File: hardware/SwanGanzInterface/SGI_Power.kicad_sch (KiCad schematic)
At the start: 21 parts, among them IC1 LM2937ET-3.3_NOPB, IC2 LM2937ET-3.3_NOPB, IC3 LM4041CILPR, U3 OPA2350

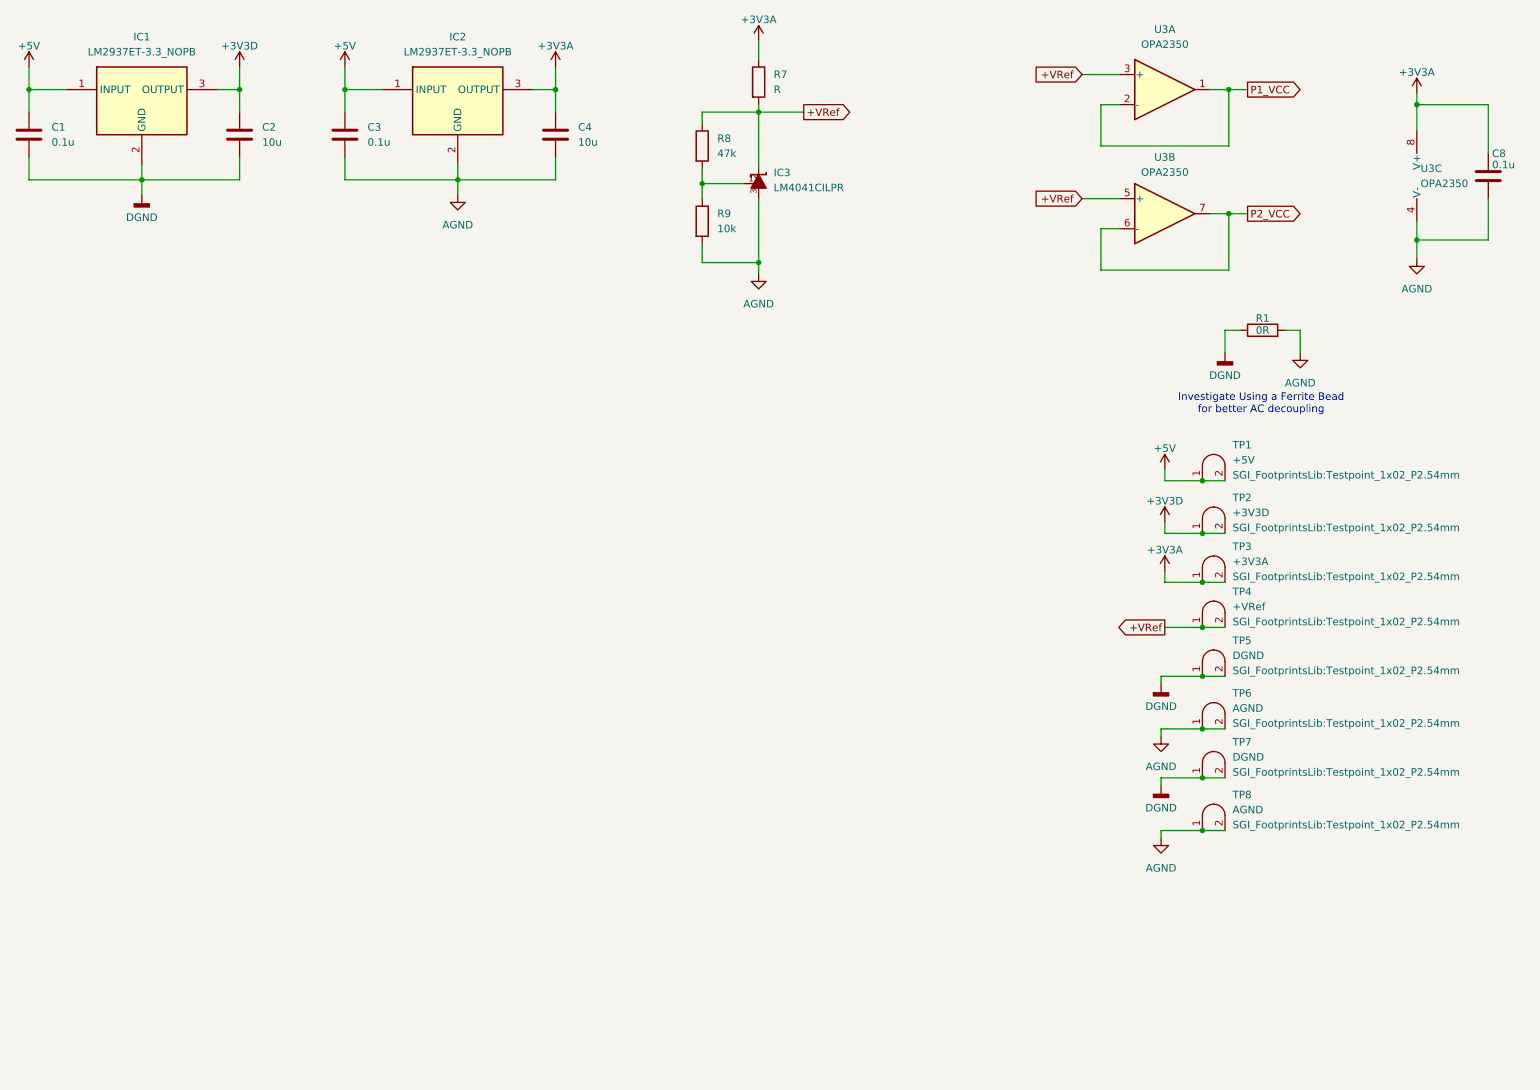
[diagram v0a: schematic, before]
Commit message: Finished MSP-LP Symbol, Started Pressure_Connector Symbol
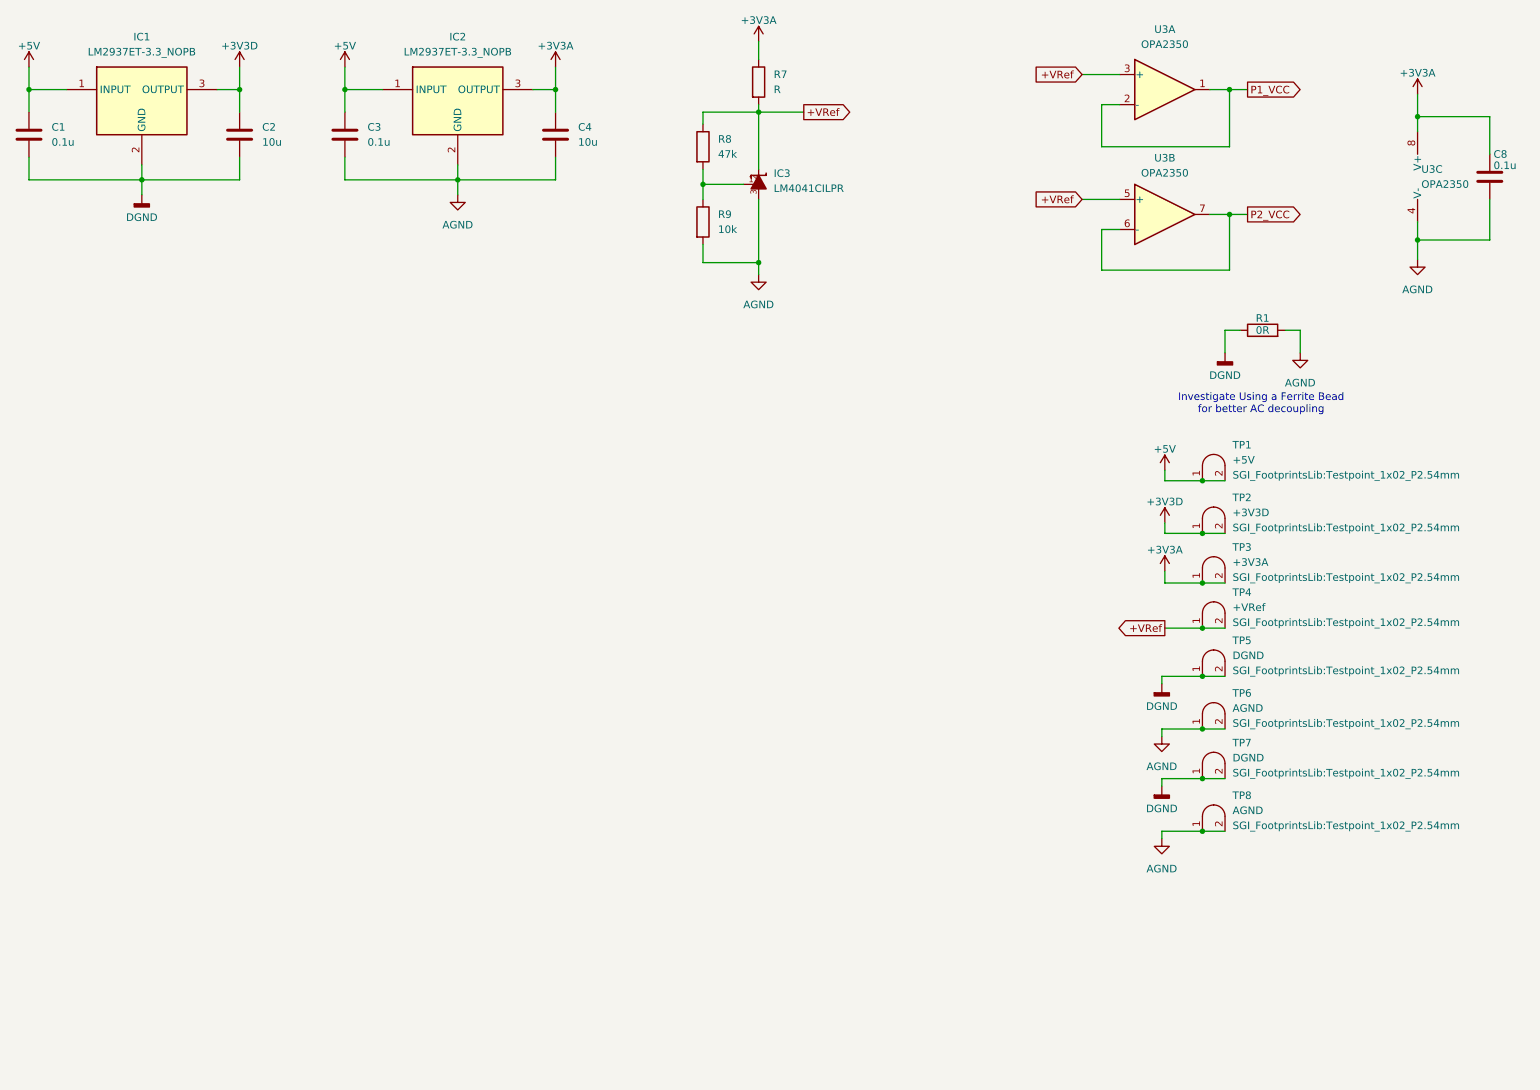
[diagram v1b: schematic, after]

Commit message: Updated gain and added power connector
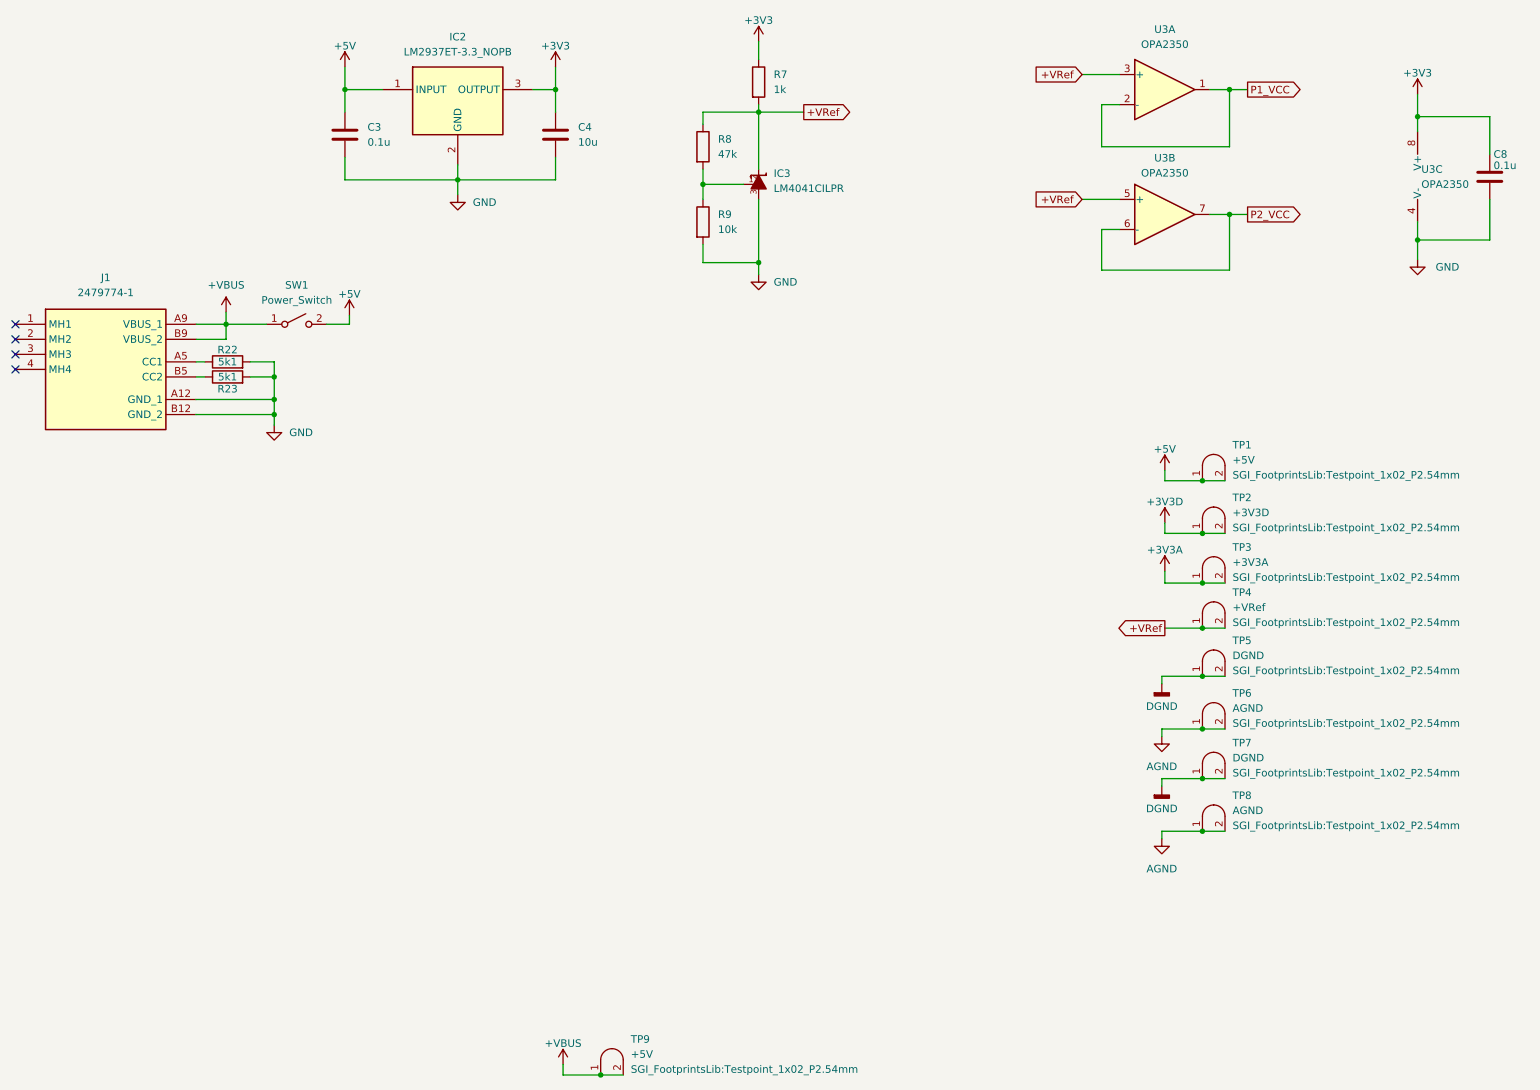
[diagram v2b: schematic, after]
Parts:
- removed C1: 0.1u, symbol Device:C
- removed C2: 10u, symbol Device:C
- removed IC1: LM2937ET-3.3_NOPB, SGI_FootprintsLib:TO254P470X1028X1955-3P, symbol SGI_SymbolLib:LM2937ET-3.3_NOPB
- removed R1: 0R, symbol Device:R
- added J1: 2479774-1, SGI_FootprintsLib:24797741, symbol SGI_SymbolLib:2479774-1
- added R22, R23: 5k1, symbol Device:R
- added SW1: Power_Switch, SGI_FootprintsLib:SW-T3-1A-A-A3-S1, symbol SGI_SymbolLib:Power_Switch
- added TP9: +5V, SGI_FootprintsLib:Testpoint_1x02_P2.54mm, symbol SGI_SymbolLib:Testpoint
- R7: value R -> 1k
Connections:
- net +3V3A: no longer C4.1, C8.1, IC2.3 (OUTPUT), R7.1, U3.8 (V+)
- net +5V: now also SW1.2 (B)
- net AGND: no longer C3.2, C4.2, C8.2, IC2.2 (GND), IC3.3, R9.2, U3.4 (V-)
- new net: J1.A5 (CC1), R22.1
- new net: J1.B5 (CC2), R23.1
- new net +3V3: C4.1, C8.1, IC2.3 (OUTPUT), R7.1, U3.8 (V+)
- new net +VBUS: J1.A9 (VBUS_1), J1.B9 (VBUS_2), SW1.1 (A), TP9.1 (A), TP9.2 (B)
- new net GND: C3.2, C4.2, C8.2, IC2.2 (GND), IC3.3, J1.A12 (GND_1), J1.B12 (GND_2), R22.2, R23.2, R9.2, U3.4 (V-)
- no-connect marks 0 -> 4
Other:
- note removed: "Investigate Using a Ferrite Bead for better AC decoupling"

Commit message: Reverse Polarity Fet, Updated Notes, Added second gain stage for pressure, General Updates
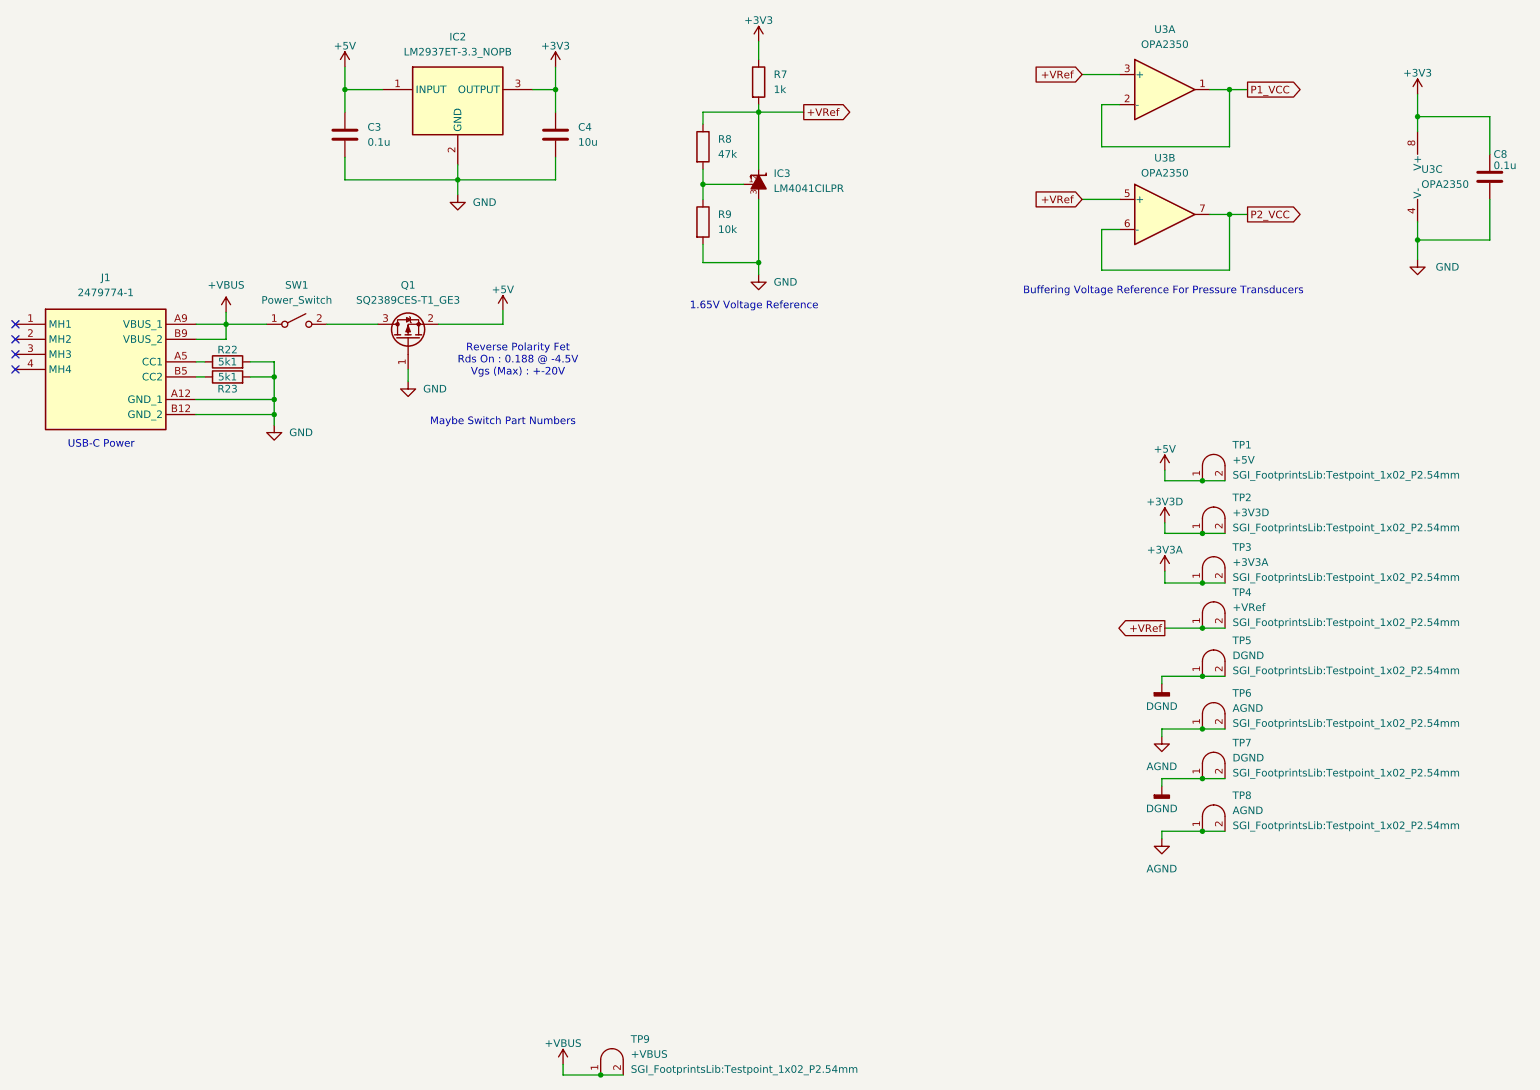
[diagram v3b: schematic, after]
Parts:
- added Q1: SQ2389CES-T1_GE3, Package_TO_SOT_SMD:SOT-23, symbol SGI_SymbolLib:SQ2389CES-T1_GE3
- TP9: value +5V -> +VBUS
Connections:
- net +5V: now also Q1.2 (S); no longer SW1.2 (B)
- net GND: now also Q1.1 (G)
- new net: Q1.3 (D), SW1.2 (B)
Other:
- note added: "1.65V Voltage Reference"
- note added: "Buffering Voltage Reference For Pressure Transducers"
- note added: "Maybe Switch Part Numbers"
- note added: "Reverse Polarity Fet Rds On : 0.188 @ -4.5V Vgs (Max) : +-20V"
- note added: "USB-C Power"
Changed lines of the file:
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@@
 		(comment 3 "Faculty Mentor - Dr. Valvano")
+	)
+	(text "Buffering Voltage Reference For Pressure Transducers"
+		(exclude_from_sim no)
+		(at 224.536 63.246 0)
+		(effects
+			(font
+				(size 1.27 1.27)
+			)
+		)
+	)
+	(text "Maybe Switch Part Numbers"
+		(exclude_from_sim no)
+		(at 113.03 85.344 0)
+		(effects
+			(font
+				(size 1.27 1.27)
+			)
+		)
+	)
+	(text "Reverse Polarity Fet\nRds On : 0.188 @ -4.5V\nVgs (Max) : +-20V"
+		(exclude_from_sim no)
+		(at 115.57 74.93 0)
+		(effects
+			(font
+				(size 1.27 1.27)
+			)
+		)
+	)
+	(text "1.65V Voltage Reference"
+		(exclude_from_sim no)
+		(at 155.448 65.786 0)
+		(effects
+			(font
+				(size 1.27 1.27)
+			)
+		)
+	)
+	(text "USB-C Power"
+		(exclude_from_sim no)
+		(at 45.212 89.154 0)
+		(effects
+			(font
+				(size 1.27 1.27)
+			)
+		)
 	)
 	(junction
@@
 	(wire
 		(pts
-			(xy 87.122 68.834) (xy 83.312 68.834)
-		)
-		(stroke
-			(width 0)
-			(type default)
-		)
-	)
-	(wire
-		(pts
 			(xy 267.462 29.972) (xy 267.462 33.782)
 		)
@@
 	(wire
 		(pts
+			(xy 97.028 78.486) (xy 97.028 76.454)
+		)
+		(stroke
+			(width 0)
+			(type default)
+		)
+	)
+	(wire
+		(pts
 			(xy 224.282 145.542) (xy 231.14 145.542)
 		)
@@
 	(wire
 		(pts
+			(xy 102.108 68.834) (xy 113.03 68.834)
+		)
+		(stroke
+			(width 0)
+			(type default)
+		)
+	)
+	(wire
+		(pts
 			(xy 231.14 112.522) (xy 234.95 112.522)
 		)
@@
 	(wire
 		(pts
-			(xy 87.122 67.31) (xy 87.122 68.834)
+			(xy 113.03 66.548) (xy 113.03 68.834)
 		)
 		(stroke
@@
 		(pts
 			(xy 61.214 71.374) (xy 66.294 71.374)
+		)
+		(stroke
+			(width 0)
+			(type default)
+		)
+	)
+	(wire
+		(pts
+			(xy 83.312 68.834) (xy 91.948 68.834)
 		)
 		(stroke
@@
 	)
 	(symbol
+		(lib_id "SGI_SymbolLib:SQ2389CES-T1_GE3")
+		(at 97.028 71.374 90)
+		(unit 1)
+		(exclude_from_sim no)
+		(in_bom yes)
+		(on_board yes)
+		(dnp no)
+		(property "Reference" "Q1"
+			(at 97.028 62.23 90)
+			(effects
+				(font
+					(size 1.27 1.27)
+				)
+			)
+		)
+		(property "Value" "SQ2389CES-T1_GE3"
+			(at 97.028 64.77 90)
+			(effects
+				(font
+					(size 1.27 1.27)
+				)
+			)
+		)
+		(property "Footprint" "Package_TO_SOT_SMD:SOT-23"
+			(at 98.933 66.294 0)
+			(effects
+				(font
+					(size 1.27 1.27)
+					(italic yes)
+				)
+				(justify left)
+				(hide yes)
+			)
+		)
+		(property "Datasheet" "kicad-embed://sq2389ces.pdf"
+			(at 100.838 66.294 0)
+			(effects
+				(font
+					(size 1.27 1.27)
+				)
+				(justify left)
+				(hide yes)
+			)
+		)
+		(property "Description" "-0.18A Id, -60V Vds, P-Channel MOSFET, SOT-23"
+			(at 97.028 71.374 0)
+			(effects
+				(font
+					(size 1.27 1.27)
+				)
+				(hide yes)
+			)
+		)
+		(pin "3"
+		)
+		(pin "2"
+		)
+		(pin "1"
+		)
+		(instances
+			(project ""
+				(path "/4e9a6e30-f660-472b-9696-bea1f34b4545/090a1e64-9482-4912-b352-6eea35714559"
+					(reference "Q1")
+					(unit 1)
+				)
+			)
+		)
+	)
+	(symbol
 		(lib_id "power:+3V3")
 		(at 224.79 102.362 0)
@@
 			)
 		)
-		(property "Value" "+5V"
+		(property "Value" "+VBUS"
 			(at 134.62 192.0873 0)
 			(effects
@@
 	)
 	(symbol
+		(lib_id "power:GNDA")
+		(at 97.028 78.486 0)
+		(unit 1)
+		(exclude_from_sim no)
+		(in_bom yes)
+		(on_board yes)
+		(dnp no)
+		(fields_autoplaced yes)
+		(property "Reference" "#PWR050"
+			(at 97.028 84.836 0)
+			(effects
+				(font
+					(size 1.27 1.27)
+				)
+				(hide yes)
+			)
+		)
+		(property "Value" "GND"
+			(at 99.568 79.7559 0)
+			(effects
+				(font
+					(size 1.27 1.27)
+				)
+				(justify left)
+			)
+		)
+		(property "Footprint" ""
+			(at 97.028 78.486 0)
+			(effects
+				(font
+					(size 1.27 1.27)
+				)
+				(hide yes)
+			)
+		)
+		(property "Datasheet" ""
+			(at 97.028 78.486 0)
+			(effects
+				(font
+					(size 1.27 1.27)
+				)
+				(hide yes)
+			)
+		)
+		(property "Description" "Power symbol creates a global label with name \"GNDA\" , analog ground"
+			(at 97.028 78.486 0)
+			(effects
+				(font
+					(size 1.27 1.27)
+				)
+				(hide yes)
+			)
+		)
+		(pin "1"
+		)
+		(instances
+			(project "SwanGanzInterface"
+				(path "/4e9a6e30-f660-472b-9696-bea1f34b4545/090a1e64-9482-4912-b352-6eea35714559"
+					(reference "#PWR050")
+					(unit 1)
+				)
+			)
+		)
+	)
+	(symbol
 		(lib_id "power:+3V3")
 		(at 86.36 25.4 0)
@@
 	(symbol
 		(lib_id "power:+3V3")
-		(at 87.122 67.31 0)
+		(at 113.03 66.548 0)
 		(unit 1)
 		(exclude_from_sim no)
@@
 		(dnp no)
 		(property "Reference" "#PWR047"
-			(at 87.122 71.12 0)
+			(at 113.03 70.358 0)
 			(effects
 				(font
@@
 		)
 		(property "Value" "+5V"
-			(at 87.122 63.754 0)
+			(at 113.03 62.992 0)
 			(effects
 				(font
@@
 		)
 		(property "Footprint" ""
-			(at 87.122 67.31 0)
+			(at 113.03 66.548 0)
 			(effects
 				(font
@@
 		)
 		(property "Datasheet" ""
-			(at 87.122 67.31 0)
+			(at 113.03 66.548 0)
 			(effects
 				(font
@@
 		)
 		(property "Description" "Power symbol creates a global label with name \"+3V3\""
-			(at 87.122 67.31 0)
-			(effects
-				(font
+			(at 113.03 66.548 0)
+			(effects
+				(font
